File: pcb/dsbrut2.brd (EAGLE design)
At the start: 51.6 x 38 mm, 18 parts, among them IC1 4175D, IC2 74HC125D, IC3 MEGA8-AI

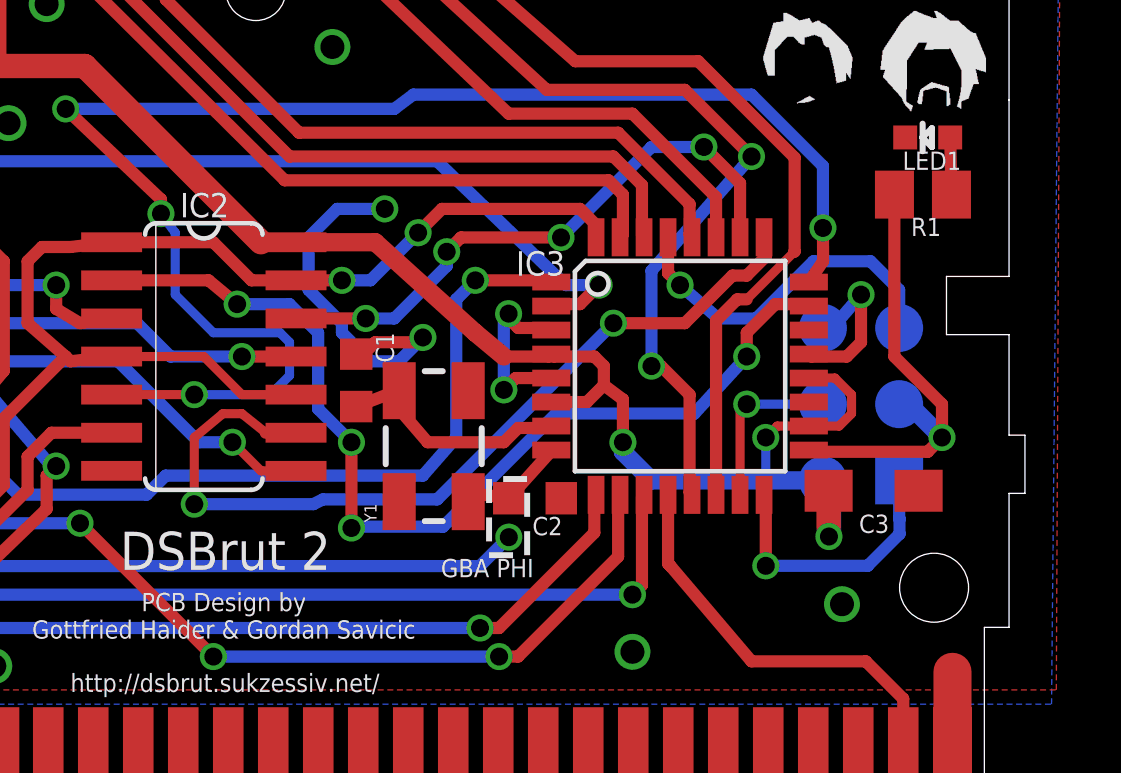
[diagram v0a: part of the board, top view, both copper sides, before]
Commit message: Label Xtal caps as 18uF, moving a few labels
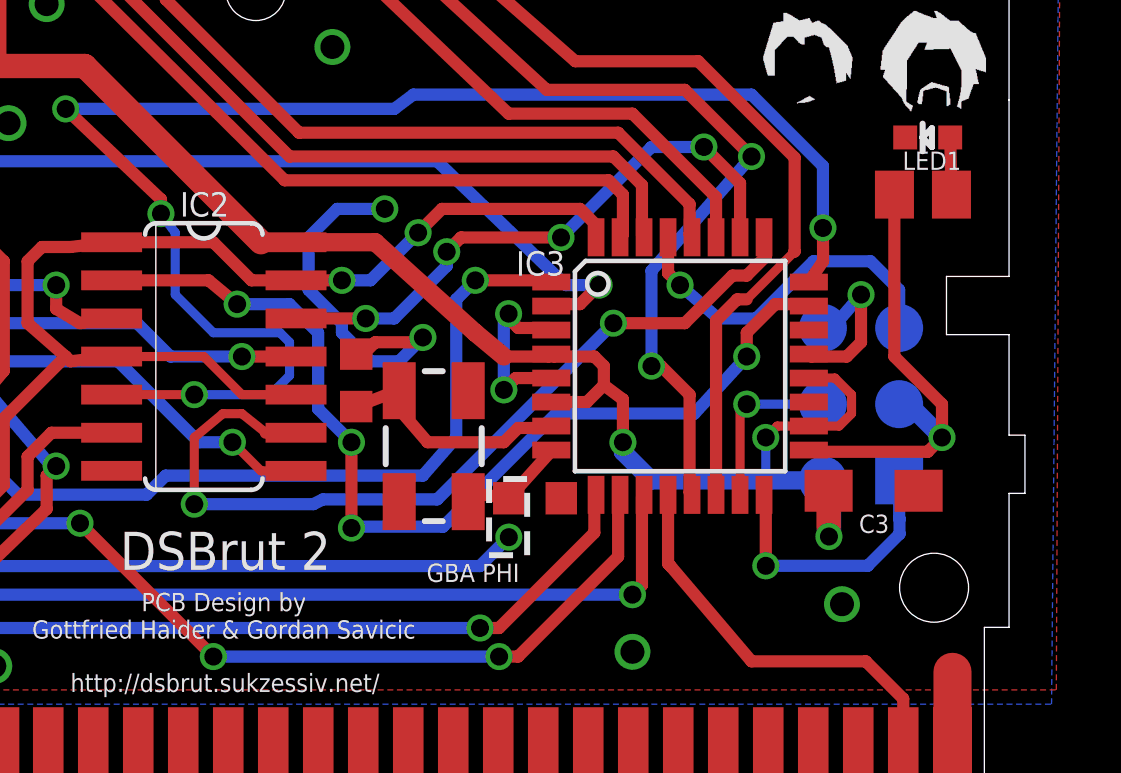
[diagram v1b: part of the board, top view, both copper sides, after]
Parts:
- C1, C2: value 10pf -> 18pF
- R1: value 220r -> 220
- Y1: value (none) -> X1
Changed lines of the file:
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@@
 <text x="30.95625" y="37.1475" size="0.6096" layer="25" rot="SR180" align="center">PB2</text>
 <rectangle x1="0" y1="0" x2="48.895" y2="6.0325" layer="42"/>
-<text x="33.8566375" y="11.192525" size="0.6096" layer="25" rot="R180">GBA PHI</text>
+<text x="33.3803875" y="11.033775" size="0.6096" layer="25" rot="R180">GBA PHI</text>
 <wire x1="32.3684875" y1="13.8557" x2="32.3684875" y2="11.3157" width="0.2" layer="25" style="shortdash"/>
 <wire x1="32.3684875" y1="11.3157" x2="33.6384875" y2="11.3157" width="0.2" layer="25" style="shortdash"/>
@@
 </element>
 <element name="IC2" library="74xx-eu" package="SO14" value="74HC125D" x="22.86" y="17.93875" smashed="yes" rot="R270">
-<attribute name="NAME" x="22.0678625" y="22.578071875" size="0.8128" layer="25" ratio="10"/>
+<attribute name="VALUE" x="22.86" y="17.907" size="0.8128" layer="27" ratio="10" rot="R90" align="center"/>
+<attribute name="NAME" x="22.06625" y="22.606" size="0.8128" layer="25" ratio="10"/>
 </element>
 <element name="JP1" library="SparkFun-Connectors" package="1X08_LONGPADS" value="" x="15.686540625" y="34.56710625" smashed="yes">
@@
 <attribute name="VALUE" x="47.625" y="27.14625" size="1.27" layer="27" rot="R180"/>
 </element>
-<element name="R1" library="rcl" package="M0805" value="220r" x="46.83125" y="23.33625" smashed="yes">
-<attribute name="NAME" x="46.4337375" y="21.95703125" size="0.6096" layer="25"/>
-<attribute name="VALUE" x="45.56125" y="20.79625" size="1.27" layer="27"/>
+<element name="R1" library="rcl" package="M0805" value="220" x="46.83125" y="23.33625" smashed="yes">
+<attribute name="VALUE" x="46.19625" y="21.59" size="0.6096" layer="27"/>
 </element>
 <element name="F1" library="dp_devices" package="L1812" value="F1" x="2.69875" y="22.70125" smashed="yes" rot="R270">
 <attribute name="NAME" x="2.10375" y="25.46125" size="0.8128" layer="25" ratio="10"/>
-<attribute name="VALUE" x="-0.67625" y="25.20125" size="1.27" layer="27" font="vector" ratio="10" rot="R270"/>
-</element>
-<element name="Y1" library="SparkFun-FreqCtrl" package="CRYSTAL-SMD-5X3" value="" x="30.523178125" y="14.950440625" rot="R90"/>
-<element name="C1" library="rcl" package="C0603K" value="10pf" x="27.94" y="17.145" smashed="yes" rot="R270">
-<attribute name="NAME" x="28.59" y="18.73875" size="0.6096" layer="25" rot="R270"/>
-<attribute name="VALUE" x="26.29" y="17.945" size="1.016" layer="27" rot="R270"/>
-</element>
-<element name="C2" library="rcl" package="C0603K" value="10pf" x="33.900084375" y="13.21485" smashed="yes" rot="R180">
-<attribute name="NAME" x="34.81565625" y="12.59151875" size="0.6096" layer="25" rot="R180"/>
-<attribute name="VALUE" x="34.700084375" y="14.86485" size="1.016" layer="27" rot="R180"/>
+</element>
+<element name="Y1" library="SparkFun-FreqCtrl" package="CRYSTAL-SMD-5X3" value="X1" x="30.523178125" y="14.950440625" smashed="yes" rot="R90">
+<attribute name="VALUE" x="30.523178125" y="14.950440625" size="0.8128" layer="27" rot="R90" align="center"/>
+</element>
+<element name="C1" library="rcl" package="C0603K" value="18pF" x="27.94" y="17.145" smashed="yes" rot="R270">
+<attribute name="VALUE" x="28.83" y="19.69125" size="0.6096" layer="27" rot="R270"/>
+</element>
+<element name="C2" library="rcl" package="C0603K" value="18pF" x="33.900084375" y="13.21485" smashed="yes" rot="R180">
+<attribute name="VALUE" x="35.652584375" y="12.4836" size="0.6096" layer="27" rot="R180"/>
 </element>
 <element name="C3" library="rcl" package="SMC_A" value="" x="45.18786875" y="13.4645375" smashed="yes">

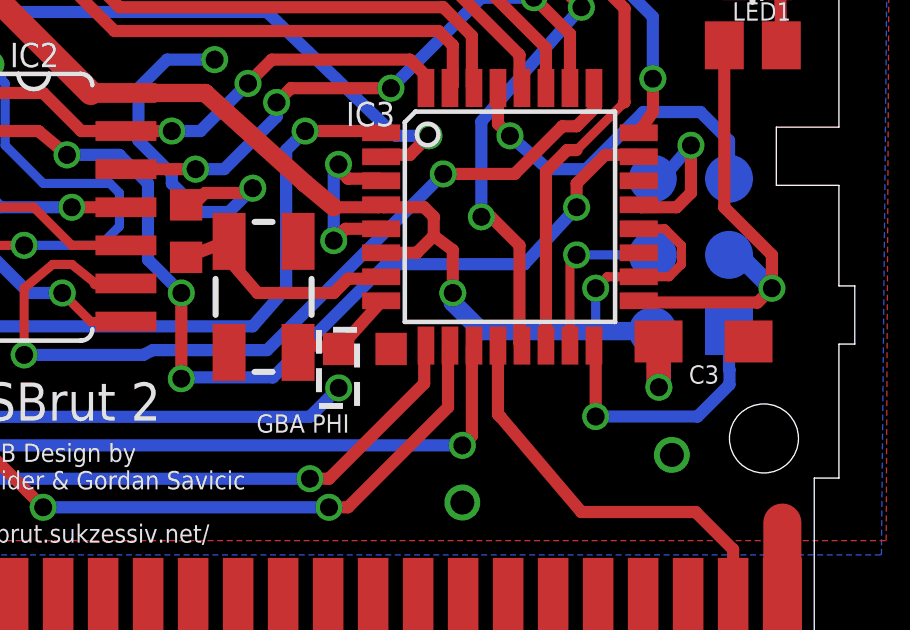
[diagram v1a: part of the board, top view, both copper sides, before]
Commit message: Changed 18pF to 8pF, labeled C3 as 10uF
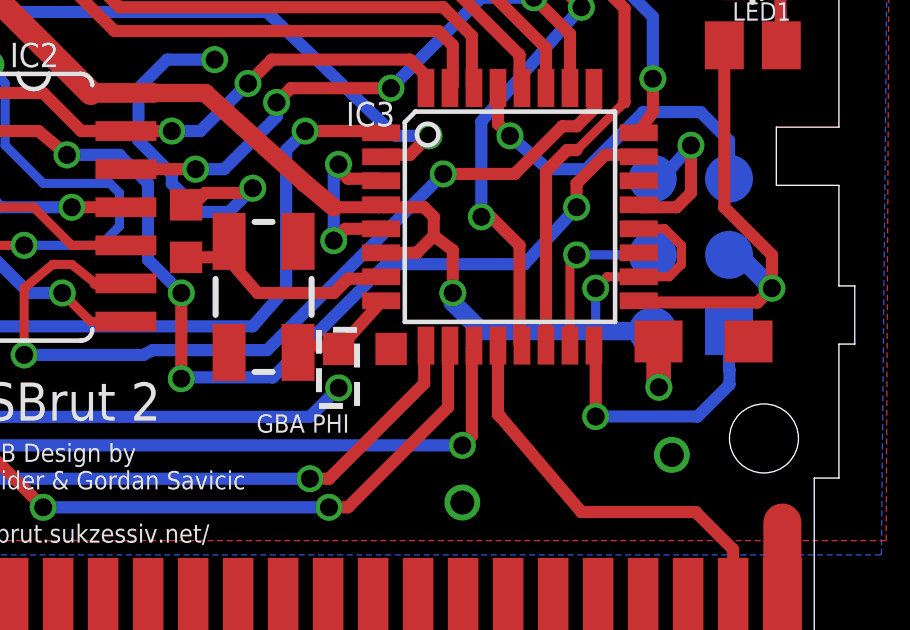
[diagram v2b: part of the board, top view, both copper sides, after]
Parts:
- C1, C2: value 18pF -> 8pF
- C3: value (none) -> 10uF
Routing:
- net N$3: track 7.96 -> 8.54 mm
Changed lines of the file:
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@@
 <attribute name="VALUE" x="30.523178125" y="14.950440625" size="0.8128" layer="27" rot="R90" align="center"/>
 </element>
-<element name="C1" library="rcl" package="C0603K" value="18pF" x="27.94" y="17.145" smashed="yes" rot="R270">
-<attribute name="VALUE" x="28.83" y="19.69125" size="0.6096" layer="27" rot="R270"/>
+<element name="C1" library="rcl" package="C0603K" value="8pF" x="27.94" y="17.145" smashed="yes" rot="R270">
+<attribute name="VALUE" x="28.83" y="19.37375" size="0.6096" layer="27" rot="R270"/>
 </element>
-<element name="C2" library="rcl" package="C0603K" value="18pF" x="33.900084375" y="13.21485" smashed="yes" rot="R180">
-<attribute name="VALUE" x="35.652584375" y="12.4836" size="0.6096" layer="27" rot="R180"/>
+<element name="C2" library="rcl" package="C0603K" value="8pF" x="33.900084375" y="13.21485" smashed="yes" rot="R180">
+<attribute name="VALUE" x="35.335084375" y="12.4836" size="0.6096" layer="27" rot="R180"/>
 </element>
-<element name="C3" library="rcl" package="SMC_A" value="" x="45.18786875" y="13.4645375" smashed="yes">
-<attribute name="NAME" x="44.69911875" y="12.0582875" size="0.6096" layer="25"/>
-<attribute name="VALUE" x="43.58786875" y="11.4645375" size="1.016" layer="27"/>
+<element name="C3" library="rcl" package="SMC_A" value="10uF" x="45.18786875" y="13.4645375" smashed="yes">
+<attribute name="VALUE" x="44.22286875" y="11.9407875" size="0.6096" layer="27"/>
 </element>
 </elements>
@@
 <contactref element="C1" pad="2"/>
 <wire x1="29.373178125" y1="16.800440625" x2="29.23625" y2="16.7725" width="0.4064" layer="1"/>
-<wire x1="29.23625" y1="16.7725" x2="27.94" y2="16.27" width="0.4064" layer="1"/>
 <wire x1="29.373178125" y1="16.800440625" x2="29.33" y2="16.23125" width="0.4064" layer="1"/>
 <wire x1="29.33" y1="16.23125" x2="30.32125" y2="15.08125" width="0.4064" layer="1"/>
@@
 <wire x1="33.3375" y1="15.5575" x2="34.37865" y2="15.5575" width="0.4064" layer="1"/>
 <wire x1="34.37865" y1="15.5575" x2="34.4424" y2="15.62125" width="0.4064" layer="1"/>
+<wire x1="27.94" y1="16.27" x2="29.373178125" y2="16.27" width="0.4064" layer="1"/>
+<wire x1="29.373178125" y1="16.27" x2="29.373178125" y2="16.800440625" width="0.4064" layer="1"/>
 </signal>
 </signals>

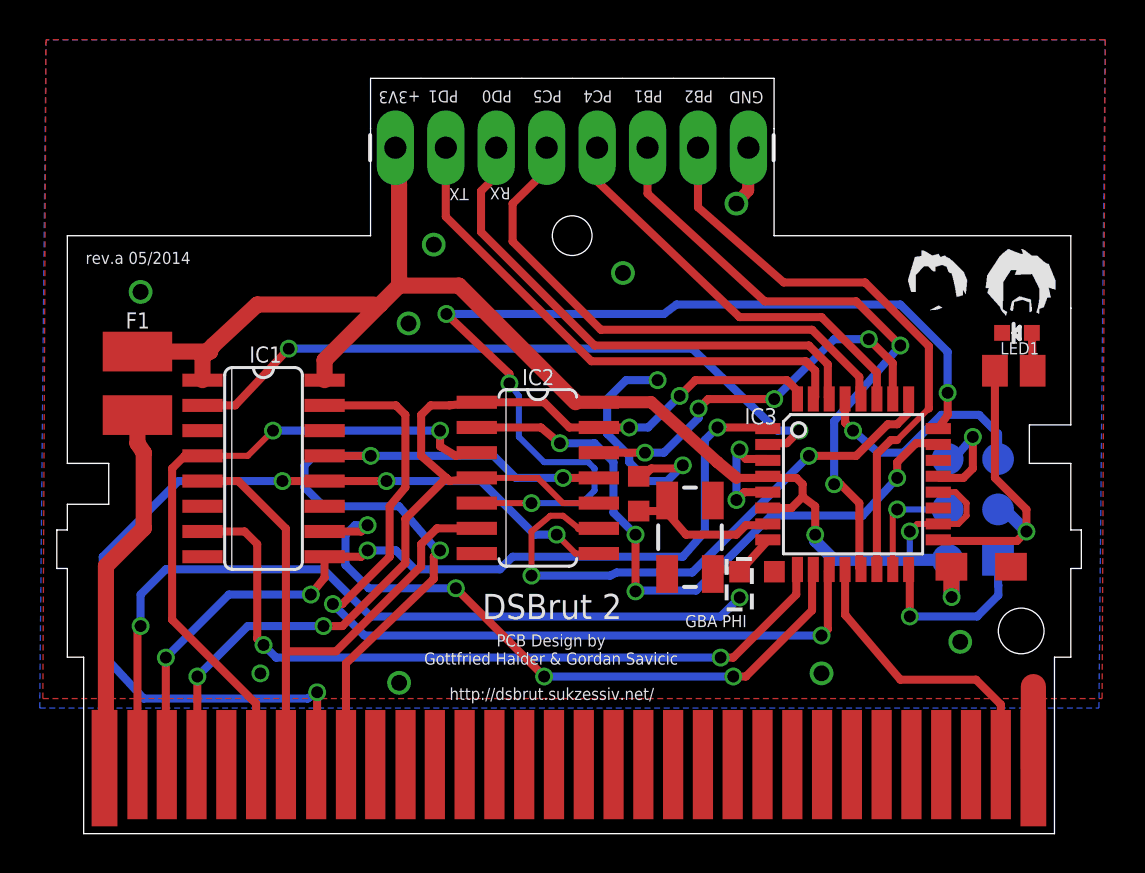
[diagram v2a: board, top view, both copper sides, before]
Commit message: changed soldermask of gba2 bridge, added gerber files, added CAM file for dsbrut2, zip file for order in sexy bash script
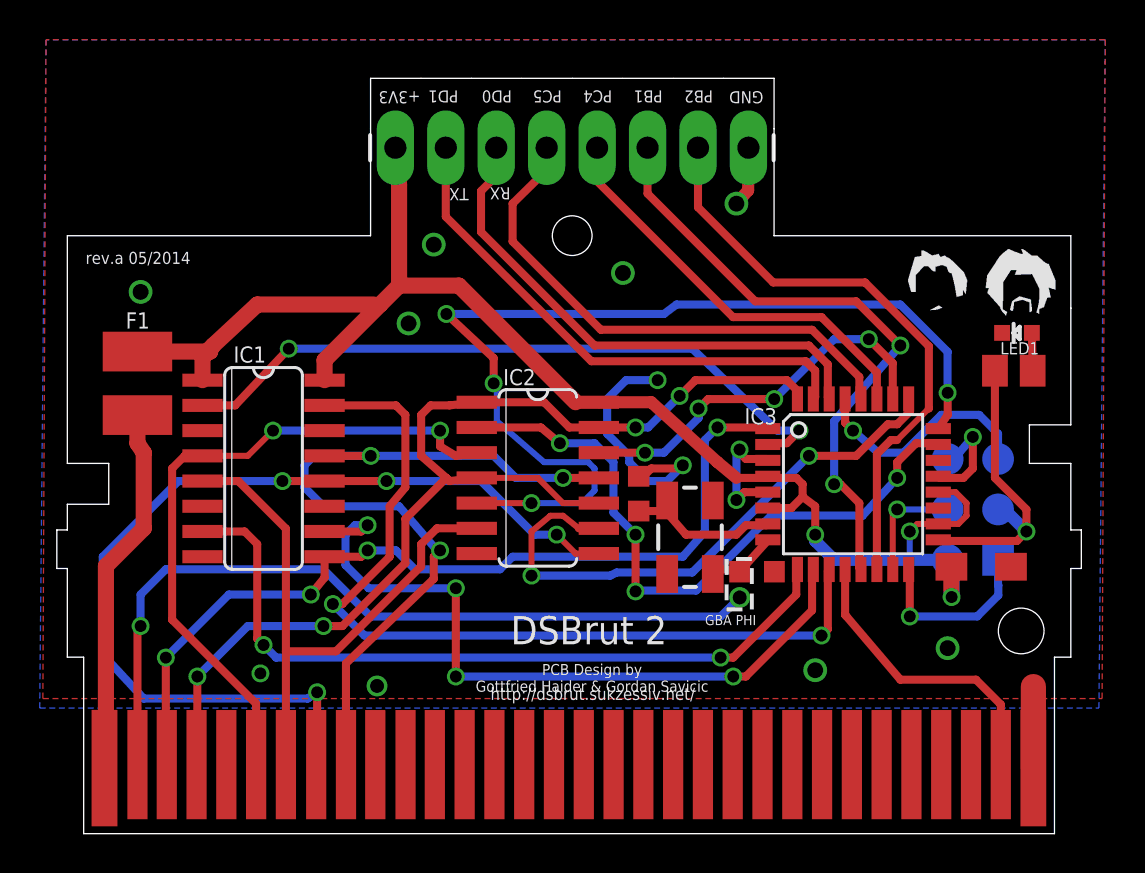
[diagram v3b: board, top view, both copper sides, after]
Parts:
- R1: value 220 -> 220R
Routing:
- net PD6: track 34.4 -> 37.0 mm

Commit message: Swap ICSP pads on the bottom, add some keepouts
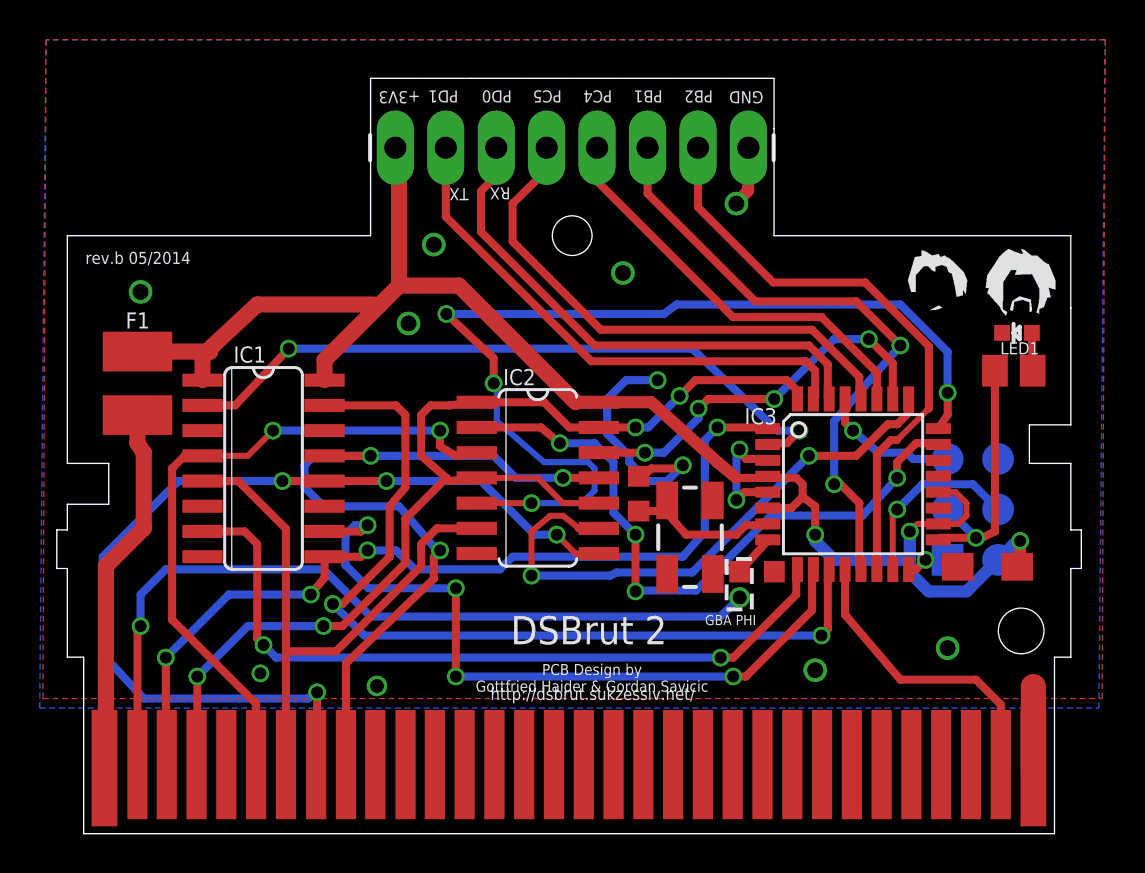
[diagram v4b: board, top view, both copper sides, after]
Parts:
- moved TP1 2.54 mm to (46.0, 13.8)
- moved TP2 2.54 mm to (46.0, 16.4)
- moved TP3 2.54 mm to (43.5, 13.8), turned to 270 degrees
- moved TP4 2.54 mm to (43.5, 16.4)
- moved TP5 2.54 mm to (43.5, 18.9)
- moved TP6 2.54 mm to (46.0, 18.9)
- moved C3 0.32 mm to (45.5, 13.5), turned to 180 degrees
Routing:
- net MISO: track 9.08 -> 2.16 mm
- net GND: track 30.7 -> 25.5 mm, vias 14 -> 13
- net RST: track 11.9 -> 7.07 mm
- net +3V3: track 75.6 -> 79.5 mm
- net MOSI: track 5.65 -> 9.25 mm
- net SCK: track 15.3 -> 13.2 mm
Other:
- board text added: "rev.b 05/2014"
- board text removed: "rev.a 05/2014"
